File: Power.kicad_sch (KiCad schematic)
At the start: 20 parts, among them U1 AMS1117-5.0, U2 AMS1117-3.3, X1 PEDAL_COMBO_TOP

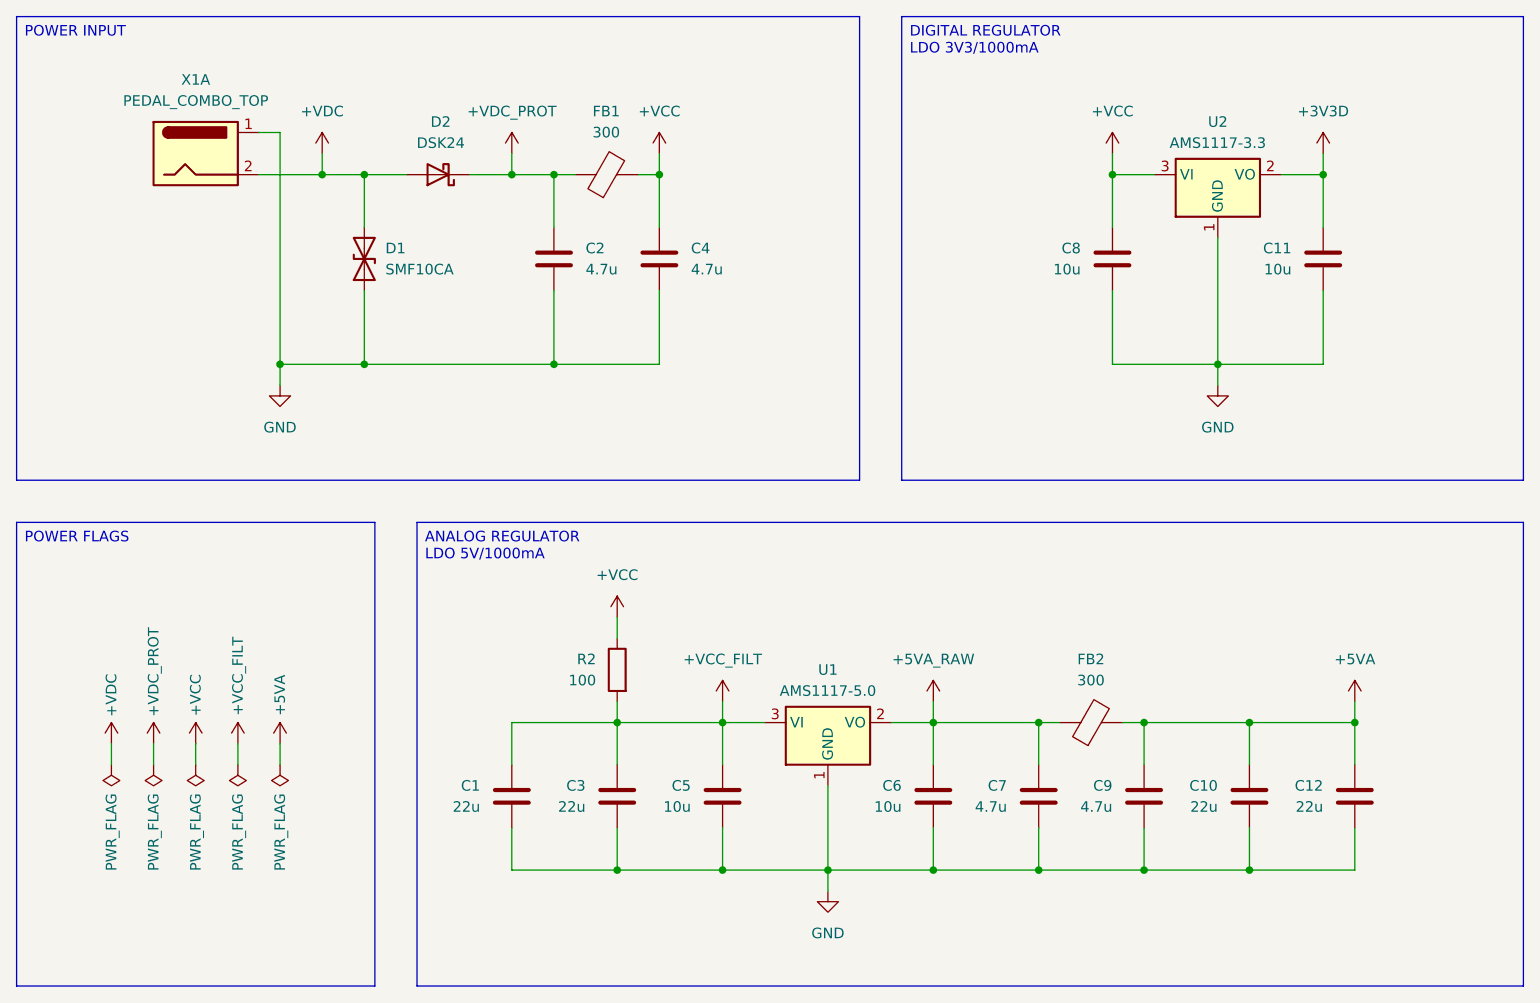
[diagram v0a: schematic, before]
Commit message: Input buffer and power
Updated the input buffer layout.
Updated the power supply layout.
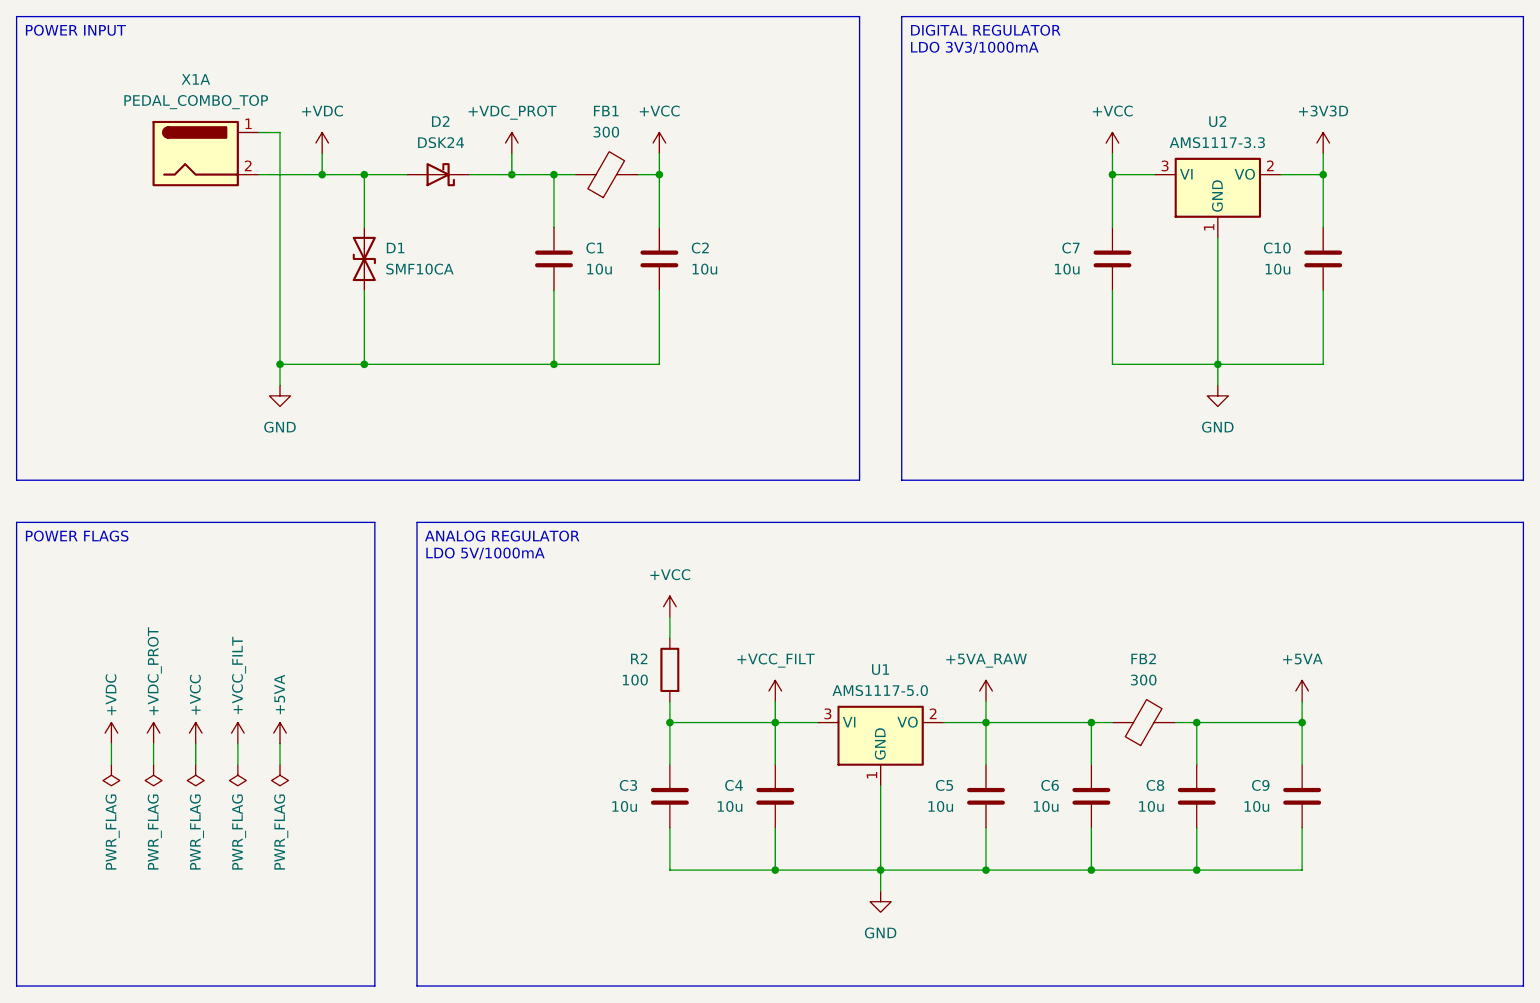
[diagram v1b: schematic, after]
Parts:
- removed C1, C12: 22u, Capacitor_SMD:C_1206_3216Metric, symbol Device:C
- C1: renamed from C2; value 4.7u -> 10u; footprint Capacitor_SMD:C_1206_3216Metric -> Capacitor_SMD:C_0805_2012Metric
- C10: renamed from C11; footprint Capacitor_SMD:C_1206_3216Metric -> Capacitor_SMD:C_0805_2012Metric
- C2: renamed from C4; value 4.7u -> 10u; footprint Capacitor_SMD:C_1206_3216Metric -> Capacitor_SMD:C_0805_2012Metric
- C3: value 22u -> 10u; footprint Capacitor_SMD:C_1206_3216Metric -> Capacitor_SMD:C_0805_2012Metric
- C4: renamed from C5; footprint Capacitor_SMD:C_1206_3216Metric -> Capacitor_SMD:C_0805_2012Metric
- C5: renamed from C6; footprint Capacitor_SMD:C_1206_3216Metric -> Capacitor_SMD:C_0805_2012Metric
- C6: renamed from C7; value 4.7u -> 10u; footprint Capacitor_SMD:C_1206_3216Metric -> Capacitor_SMD:C_0805_2012Metric
- C7: renamed from C8; footprint Capacitor_SMD:C_1206_3216Metric -> Capacitor_SMD:C_0805_2012Metric
- C8: renamed from C9; value 4.7u -> 10u; footprint Capacitor_SMD:C_1206_3216Metric -> Capacitor_SMD:C_0805_2012Metric
- C9: renamed from C10; value 22u -> 10u; footprint Capacitor_SMD:C_1206_3216Metric -> Capacitor_SMD:C_0805_2012Metric
- FB1, FB2: footprint Inductor_SMD:L_0805_2012Metric -> Inductor_SMD:L_0603_1608Metric
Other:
- moved on the sheet: C3, C4, C5, C6, C8, C9, FB2, R2, U1
